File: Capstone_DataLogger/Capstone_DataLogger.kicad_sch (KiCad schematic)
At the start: 0 parts

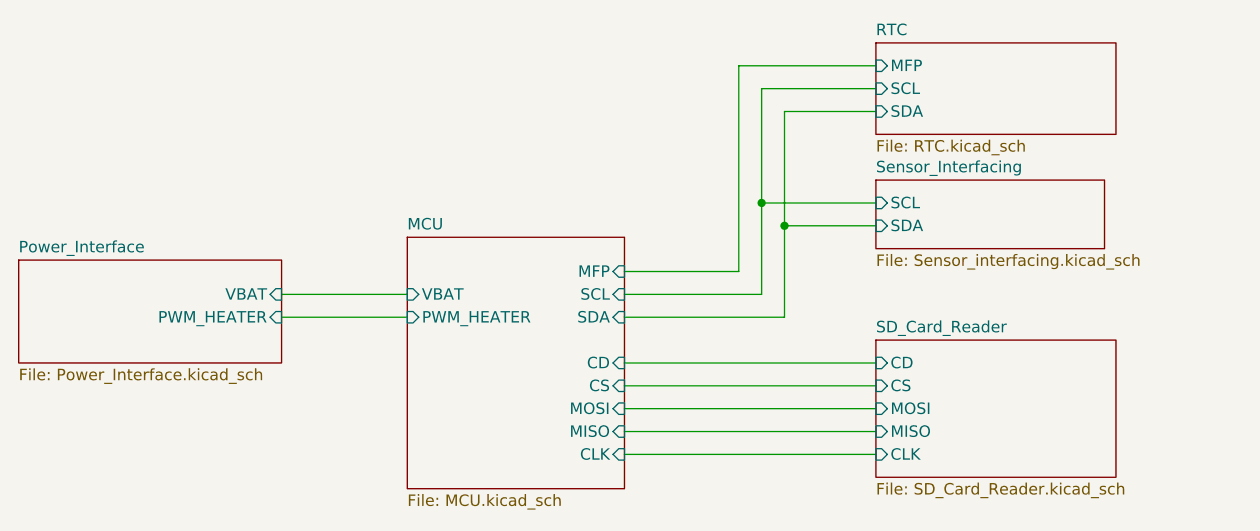
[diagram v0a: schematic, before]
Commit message: pcb connected except SD card
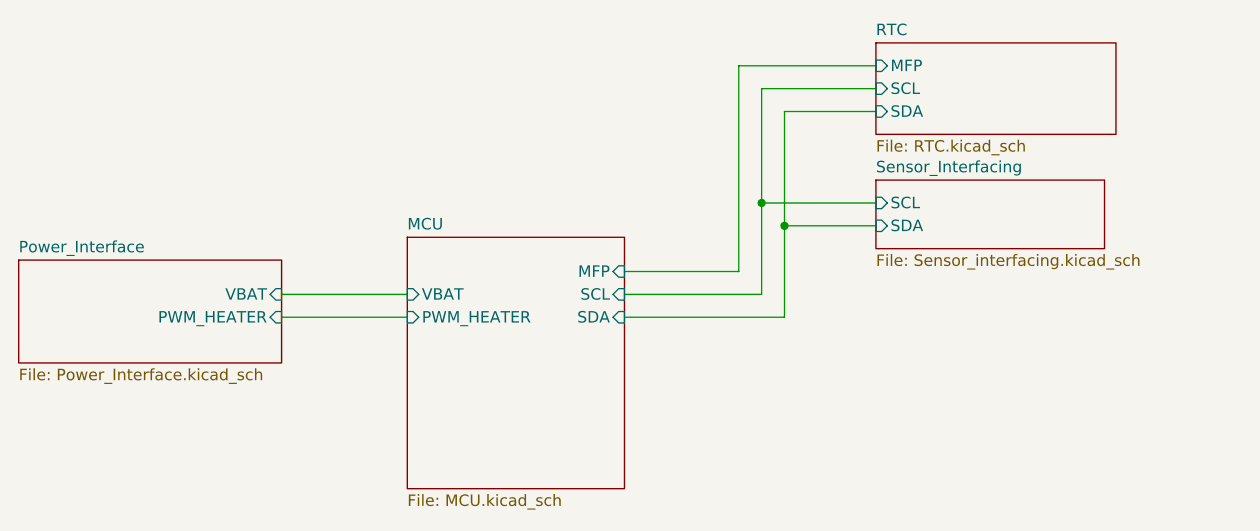
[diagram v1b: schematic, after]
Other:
- removed sheet SD_Card_Reader
- sheet MCU ports: added none; removed CD, CLK, CS, MISO, MOSI
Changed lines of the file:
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@@
-	(wire
-		(pts
-			(xy 149.86 109.22) (xy 177.8 109.22)
-		)
-		(stroke
-			(width 0)
-			(type default)
-		)
-	)
 	(wire
 		(pts
@@
 	(wire
 		(pts
-			(xy 149.86 104.14) (xy 177.8 104.14)
-		)
-		(stroke
-			(width 0)
-			(type default)
-		)
-	)
-	(wire
-		(pts
 			(xy 165.1 81.28) (xy 177.8 81.28)
 		)
@@
 	(wire
 		(pts
-			(xy 149.86 101.6) (xy 177.8 101.6)
-		)
-		(stroke
-			(width 0)
-			(type default)
-		)
-	)
-	(wire
-		(pts
 			(xy 167.64 83.82) (xy 177.8 83.82)
 		)
@@
 		(pts
 			(xy 162.56 66.04) (xy 177.8 66.04)
-		)
-		(stroke
-			(width 0)
-			(type default)
-		)
-	)
-	(wire
-		(pts
-			(xy 149.86 99.06) (xy 177.8 99.06)
-		)
-		(stroke
-			(width 0)
-			(type default)
-		)
-	)
-	(wire
-		(pts
-			(xy 149.86 106.68) (xy 177.8 106.68)
 		)
 		(stroke
@@
 	)
 	(sheet
-		(at 177.8 96.52)
-		(size 26.67 15.24)
-		(fields_autoplaced yes)
-		(stroke
-			(width 0.1524)
-			(type solid)
-		)
-		(fill
-			(color 0 0 0 0.0000)
-		)
-		(property "Sheetname" "SD_Card_Reader"
-			(at 177.8 95.8084 0)
-			(effects
-				(font
-					(size 1.27 1.27)
-				)
-				(justify left bottom)
-			)
-		)
-		(property "Sheetfile" "SD_Card_Reader.kicad_sch"
-			(at 177.8 112.3446 0)
-			(effects
-				(font
-					(size 1.27 1.27)
-				)
-				(justify left top)
-			)
-		)
-		(property "Field2" ""
-			(at 177.8 96.52 0)
-			(effects
-				(font
-					(size 1.27 1.27)
-				)
-				(hide yes)
-			)
-		)
-		(pin "CS" input
-			(at 177.8 101.6 180)
-			(effects
-				(font
-					(size 1.27 1.27)
-				)
-				(justify left)
-			)
-		)
-		(pin "CLK" input
-			(at 177.8 109.22 180)
-			(effects
-				(font
-					(size 1.27 1.27)
-				)
-				(justify left)
-			)
-		)
-		(pin "MOSI" input
-			(at 177.8 104.14 180)
-			(effects
-				(font
-					(size 1.27 1.27)
-				)
-				(justify left)
-			)
-		)
-		(pin "MISO" input
-			(at 177.8 106.68 180)
-			(effects
-				(font
-					(size 1.27 1.27)
-				)
-				(justify left)
-			)
-		)
-		(pin "CD" input
-			(at 177.8 99.06 180)
-			(effects
-				(font
-					(size 1.27 1.27)
-				)
-				(justify left)
-			)
-		)
-		(instances
-			(project "Capstone_DataLogger"
-				(path "/3b56a84b-c06c-4c22-a01a-903db63bf091"
-					(page "4")
-				)
-			)
-		)
-	)
-	(sheet
 		(at 82.55 87.63)
 		(size 29.21 11.43)
@@
 			)
 		)
-		(pin "CS" input
-			(at 149.86 101.6 0)
-			(effects
-				(font
-					(size 1.27 1.27)
-				)
-				(justify right)
-			)
-		)
-		(pin "CD" input
-			(at 149.86 99.06 0)
-			(effects
-				(font
-					(size 1.27 1.27)
-				)
-				(justify right)
-			)
-		)
 		(pin "SCL" input
 			(at 149.86 91.44 0)
@@
 			)
 		)
-		(pin "MOSI" input
-			(at 149.86 104.14 0)
-			(effects
-				(font
-					(size 1.27 1.27)
-				)
-				(justify right)
-			)
-		)
-		(pin "CLK" input
-			(at 149.86 109.22 0)
-			(effects
-				(font
-					(size 1.27 1.27)
-				)
-				(justify right)
-			)
-		)
 		(pin "SDA" input
 			(at 149.86 93.98 0)
@@
 			)
 		)
-		(pin "MISO" input
-			(at 149.86 106.68 0)
-			(effects
-				(font
-					(size 1.27 1.27)
-				)
-				(justify right)
-			)
-		)
